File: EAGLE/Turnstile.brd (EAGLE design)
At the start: 99.8 x 94.7 mm, 15 parts

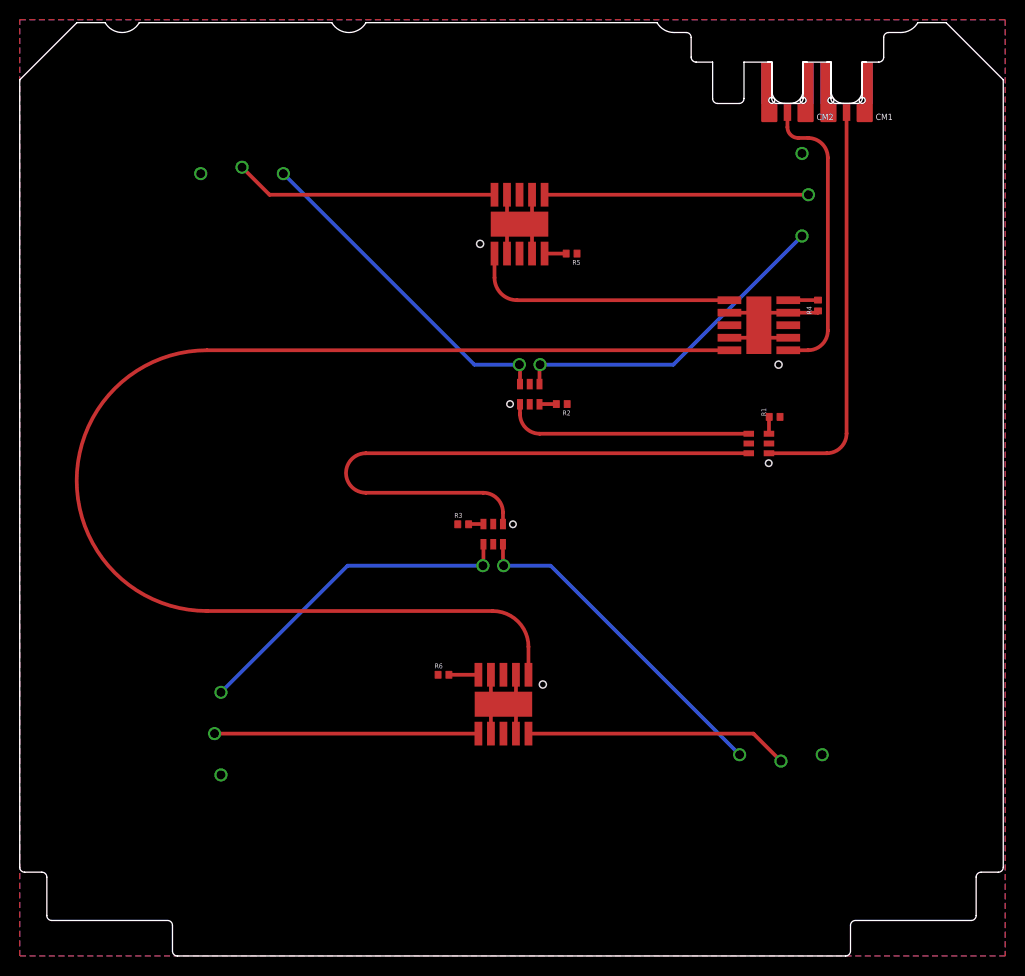
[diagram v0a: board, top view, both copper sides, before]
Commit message: OMG, there's a lot on thie board! Added main connector, solar connectors, end cap connector, and new and improved debug connector which is the best thing ever. Good luck Eric!
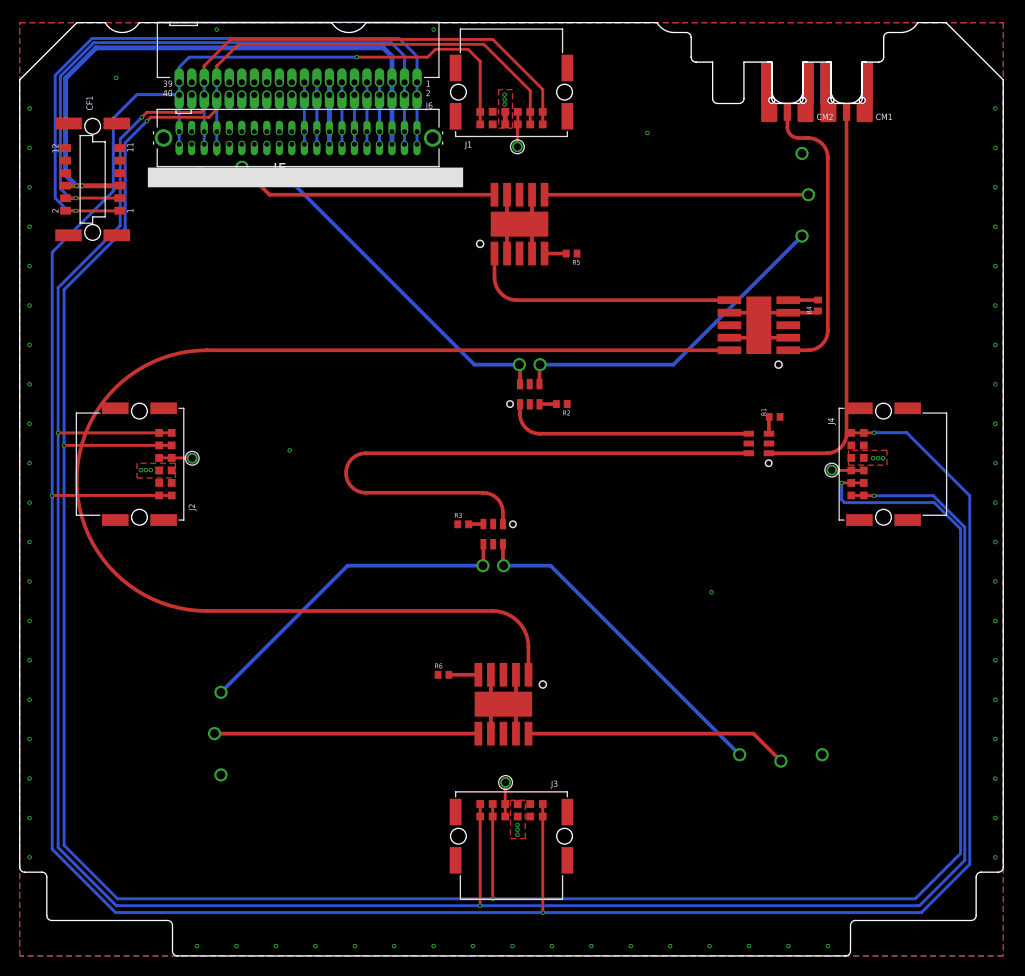
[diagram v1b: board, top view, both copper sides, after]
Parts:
- added CF1: J-HARWIN-M55-60X1242R, J-Harwin-M55-60X1242R-12pin-1.27mm-F-vertical:HARWIN-M55-60X1242R
- added J1, J2, J3, J4: Harwin M55-7101242R, J-Harwin-M55-7101242-Solar-card-connector:M55-7101242R
- added J5: SFM-120-X1-XXX-D, J-Samtec-SFM-120-X1-XXX-D:SFM-120-X1-XXX-D
- added J6: J-SAMTEC-TFM-120-X1-XXX-D-RA, J-Samtec-TFM-120-X1-XXX-D-RA:J-SAMTEC-TFM-120-X1-XXX-D-RA
- added TP1, TP2, TP3, TP4: TEST-POINT-LARGE-SQUARE, oresat-misc:1X01
- PCB1: value ORESAT-CARD-V1.1-3XRF -> ORESAT-CARD-V1.1-END-CARD-3RF-V1.0; device oresat-cards:ORESAT-CARD-V1.1-3XRF -> oresat-cards:ORESAT-CARDV1.1-END-CARD-3RF-V1.0
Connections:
- new net !SD: J1.1, J1.2, J2.1, J2.2, J3.1, J3.2, J4.1, J4.2, J5.39, J5.40, J6.39, J6.40
- new net CAN1_H: J1.10, J1.9, J2.10, J2.9, J3.10, J3.9, J4.10, J4.9, J5.33, J5.34, J6.33, J6.34
- new net CAN1_L: J1.11, J1.12, J2.11, J2.12, J3.11, J3.12, J4.11, J4.12, J5.35, J5.36, J6.35, J6.36
- new net CAN2_H: J5.17, J5.18, J6.17, J6.18
- new net CAN2_L: J5.19, J5.20, J6.19, J6.20
- new net MAG-POWER: CF1.5, CF1.6, J5.5, J5.6, J6.5, J6.6
- new net MAG-SCL: CF1.3, CF1.4, J5.3, J5.4, J6.3, J6.4
- new net MAG-SDA: CF1.1, CF1.2, J5.1, J5.2, J6.1, J6.2
- new net N$10: J4.7, J4.8, TP4.1
- new net N$7: J1.7, J1.8, TP1.1
- new net N$8: J2.7, J2.8, TP2.1
- new net N$9: J3.7, J3.8, TP3.1
- new net OPD_PWR: J5.15, J5.16, J6.15, J6.16
- new net OPD_SCL: J5.13, J5.14, J6.13, J6.14
- new net OPD_SDA: J5.11, J5.12, J6.11, J6.12
- new net SPARE2: J5.7, J5.8, J6.7, J6.8
- new net TURNSTILE-DEPLOY: J5.10, J5.9, J6.10, J6.9
- new net VBUS: J1.5, J1.6, J2.5, J2.6, J3.5, J3.6, J4.5, J4.6, J5.21, J5.22, J5.23, J5.24, J5.25, J5.26, J6.21, J6.22, J6.23, J6.24, J6.25, J6.26
- net GND: now also CF1.7, CF1.8, CF1.P$1, CF1.P$2, CF1.P$3, CF1.P$4, J1.3, J1.4, J1.P$1, J1.P$2, J1.P$3, J1.P$4, J2.3, J2.4, J2.P$1, J2.P$2, J2.P$3, J2.P$4, J3.3, J3.4, J3.P$1, J3.P$2, J3.P$3, J3.P$4, J4.3, J4.4, J4.P$1, J4.P$2, J4.P$3, J4.P$4, J5.27, J5.28, J5.29, J5.30, J5.31, J5.32, J5.37, J5.38, J5.LC1, J5.LC2, J6.27, J6.28, J6.29, J6.30, J6.31, J6.32, J6.37, J6.38
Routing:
- net !SD: track 0.00 -> 303.7 mm, vias 0 -> 4
- net CAN1_L: track 0.00 -> 299.7 mm, vias 0 -> 4
- net CAN1_H: track 0.00 -> 299.0 mm, vias 0 -> 4
- net MAG-SDA: track 0.00 -> 68.5 mm, vias 0 -> 1
- net MAG-SCL: track 0.00 -> 64.7 mm, vias 0 -> 1
- net MAG-POWER: track 0.00 -> 61.1 mm, vias 0 -> 2
- net TURNSTILE-DEPLOY: track 0.00 -> 6.27 mm
- net SPARE2: track 0.00 -> 6.27 mm
- net OPD_SDA: track 0.00 -> 6.27 mm
- net OPD_SCL: track 0.00 -> 6.27 mm
- net OPD_PWR: track 0.00 -> 6.27 mm
- net CAN2_L: track 0.00 -> 6.27 mm
- net CAN2_H: track 0.00 -> 6.27 mm
- net N$7: track 0.00 -> 3.56 mm
- net N$9: track 0.00 -> 3.48 mm
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- added copper zone on layer 1, net VBUS
- added copper zone on layer 15, net VBUS
